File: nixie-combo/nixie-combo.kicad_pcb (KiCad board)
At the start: 2 copper layers, 99 x 70 mm, 26 parts, among them P1 CONN_2, P10 CONN_1, P2 CONN_6, P3 CONN_1, P4 CONN_1, P7 CONN_1, P8 CONN_1, P9 CONN_1, U1 K155ID1, U2 K155ID1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

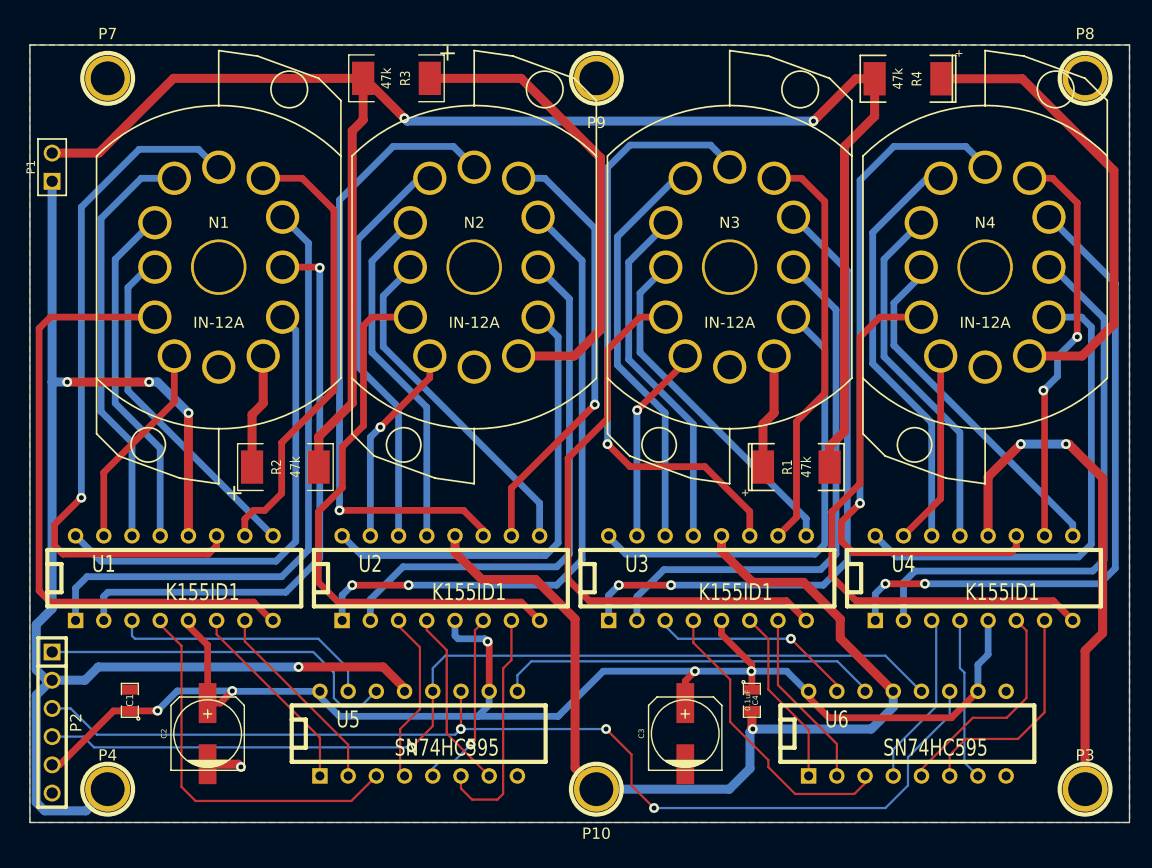
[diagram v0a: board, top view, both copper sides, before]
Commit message: nixie-combo: Improved GND plane for nixies.
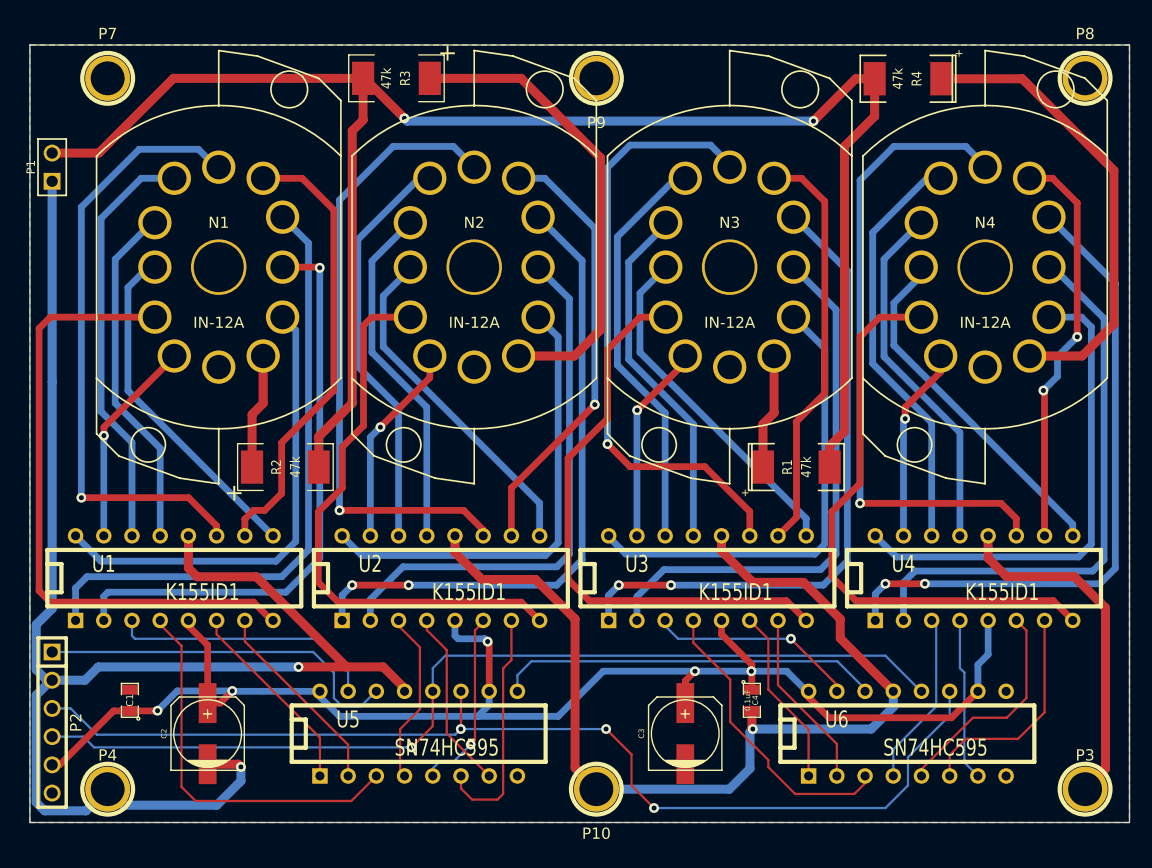
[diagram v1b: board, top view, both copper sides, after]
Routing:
- net /a6: track 62.8 -> 55.5 mm
- net /d6: track 64.0 -> 58.6 mm
- net GND: track 262.1 -> 257.9 mm, vias 8 -> 3
- net /a1: vias 0 -> 1
- net /d1: vias 0 -> 1

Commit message: nixie-combo: Increase HV clearance to 32mils.
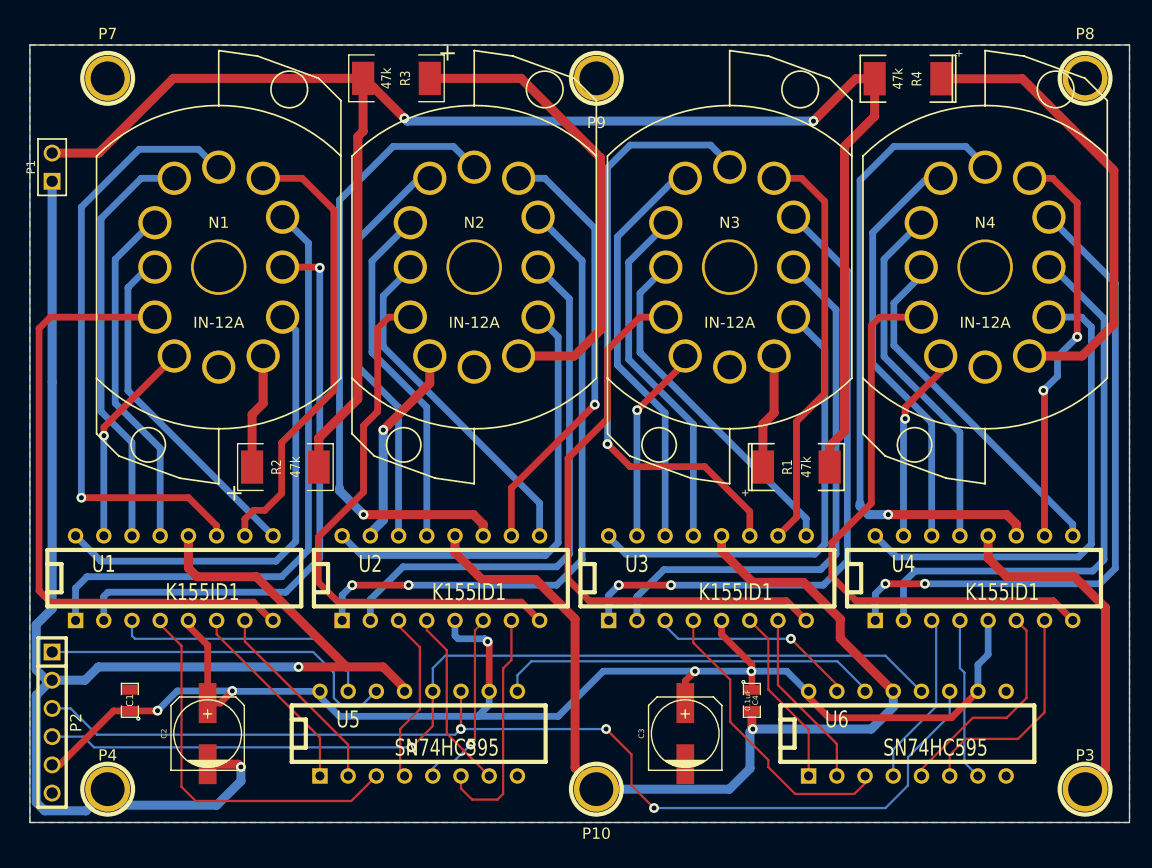
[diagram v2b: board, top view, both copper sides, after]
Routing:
- net /b2: track 50.7 -> 49.8 mm
- net /b6: track 57.0 -> 56.3 mm
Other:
- net class HV added: clearance 0.8128, trace_width 0.8128, via_dia 0.889, via_drill 0.635

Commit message: nixie-combo: Replace IN-12A with IN-12A-SOCKET.
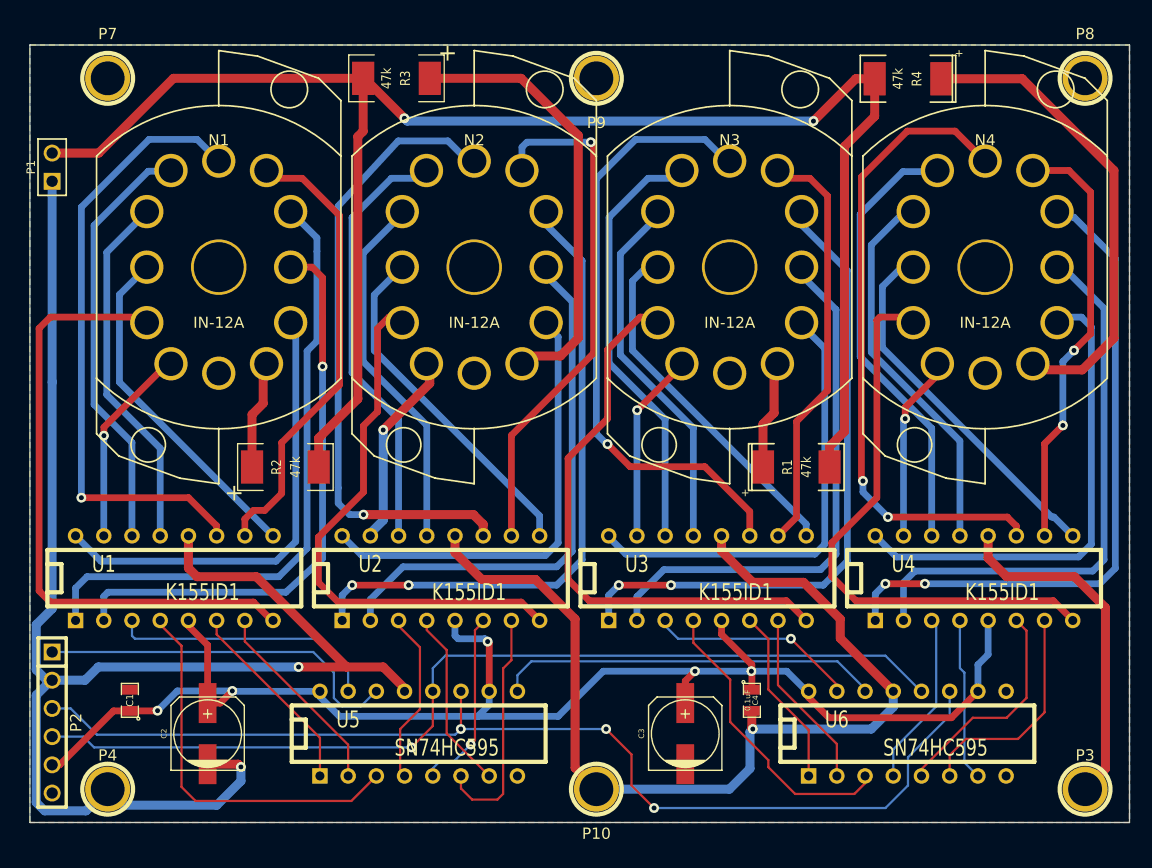
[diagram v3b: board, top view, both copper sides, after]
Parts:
- N1, N2, N3, N4: footprint IN-12A -> IN-12A-SOCKET
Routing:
- net /b7: track 39.5 -> 47.0 mm
- net /c4: track 32.0 -> 35.2 mm
- net /d5: track 37.7 -> 40.9 mm
- net N-0000032: track 42.2 -> 39.8 mm
- net /d4: track 32.4 -> 34.6 mm
- net /d7: track 36.5 -> 38.7 mm
- net /c5: track 37.0 -> 39.1 mm
- net /b5: track 37.0 -> 38.9 mm
- net /b4: track 31.7 -> 33.1 mm
- net /d8: track 59.1 -> 60.4 mm
- net /c6: track 55.2 -> 56.5 mm
- net /d3: track 31.9 -> 33.2 mm
- net N-000007: track 41.6 -> 42.8 mm
- net /a4: track 31.5 -> 32.7 mm
- net /b6: track 56.3 -> 57.4 mm
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
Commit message: nixie-combo: Add silk screen.
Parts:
- added ?: , LOGO_SNOWCAP_BACK, B.Cu at (148.2, 94.7)
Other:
- board text added: "HIGH VOLTAGE!"
- board text added: "NIXIE-COMBO v1"
